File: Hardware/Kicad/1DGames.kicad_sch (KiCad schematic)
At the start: 0 parts

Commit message: Inline accessors, small cleanups, removed empty destructors
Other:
- sheet I2S Sound (page 4) renamed Audio (page 4) (pagina 4)
- sheet players renamed TM1637 & Joysticks
- note added: "AUDIO"
- note removed: "I2S SOUND"
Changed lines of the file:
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@@
 		)
 	)
-	(text "I2S SOUND"
+	(text "AUDIO"
 		(exclude_from_sim no)
 		(at 39.624 86.868 0)
@@
 			(color 0 0 0 0)
 		)
-		(property "Sheetname" "I2S Sound (page 4)"
+		(property "Sheetname" "Audio (page 4) (pagina 4)"
 			(at 24.13 90.7284 0)
 			(show_name no)
@@
 			(color 0 0 0 0)
 		)
-		(property "Sheetname" "players"
+		(property "Sheetname" "TM1637 & Joysticks"
 			(at 167.64 81.8384 0)
 			(show_name no)

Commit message: New architecture, L1 composition finished, probably, on ESP32
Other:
- sheet ESP32 & SPI ports: added MCP23017_INT_AB; removed none
- sheet I2C ports: added MCP23017_INT_AB; removed none
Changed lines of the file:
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@@
+	(wire
+		(pts
+			(xy 165.1 50.8) (xy 196.85 50.8)
+		)
+		(stroke
+			(width 0)
+			(type default)
+		)
+	)
 	(wire
 		(pts
@@
 	(wire
 		(pts
+			(xy 19.05 185.42) (xy 19.05 208.28)
+		)
+		(stroke
+			(width 0)
+			(type default)
+		)
+	)
+	(wire
+		(pts
 			(xy 143.51 107.95) (xy 152.4 107.95)
 		)
@@
 	(wire
 		(pts
+			(xy 24.13 185.42) (xy 19.05 185.42)
+		)
+		(stroke
+			(width 0)
+			(type default)
+		)
+	)
+	(wire
+		(pts
 			(xy 67.31 96.52) (xy 50.8 96.52)
 		)
@@
 	(wire
 		(pts
+			(xy 196.85 208.28) (xy 196.85 50.8)
+		)
+		(stroke
+			(width 0)
+			(type default)
+		)
+	)
+	(wire
+		(pts
 			(xy 67.31 184.15) (xy 161.29 184.15)
 		)
@@
 		(pts
 			(xy 90.17 110.49) (xy 97.79 110.49)
+		)
+		(stroke
+			(width 0)
+			(type default)
+		)
+	)
+	(wire
+		(pts
+			(xy 19.05 208.28) (xy 196.85 208.28)
 		)
 		(stroke
@@
 			)
 		)
+		(pin "MCP23017_INT_AB" input
+			(at 24.13 185.42 180)
+			(effects
+				(font
+					(size 1.27 1.27)
+				)
+				(justify left)
+			)
+		)
 		(instances
 			(project "1DGames"
@@
 	(sheet
 		(at 167.64 82.55)
-		(size 29.21 66.04)
+		(size 26.67 66.04)
 		(exclude_from_sim no)
 		(in_bom yes)
@@
 			(effects
 				(font
+					(size 1.27 1.27)
+				)
+				(justify right)
+			)
+		)
+		(pin "MCP23017_INT_AB" input
+			(at 165.1 50.8 0)
+			(effects
+				(font

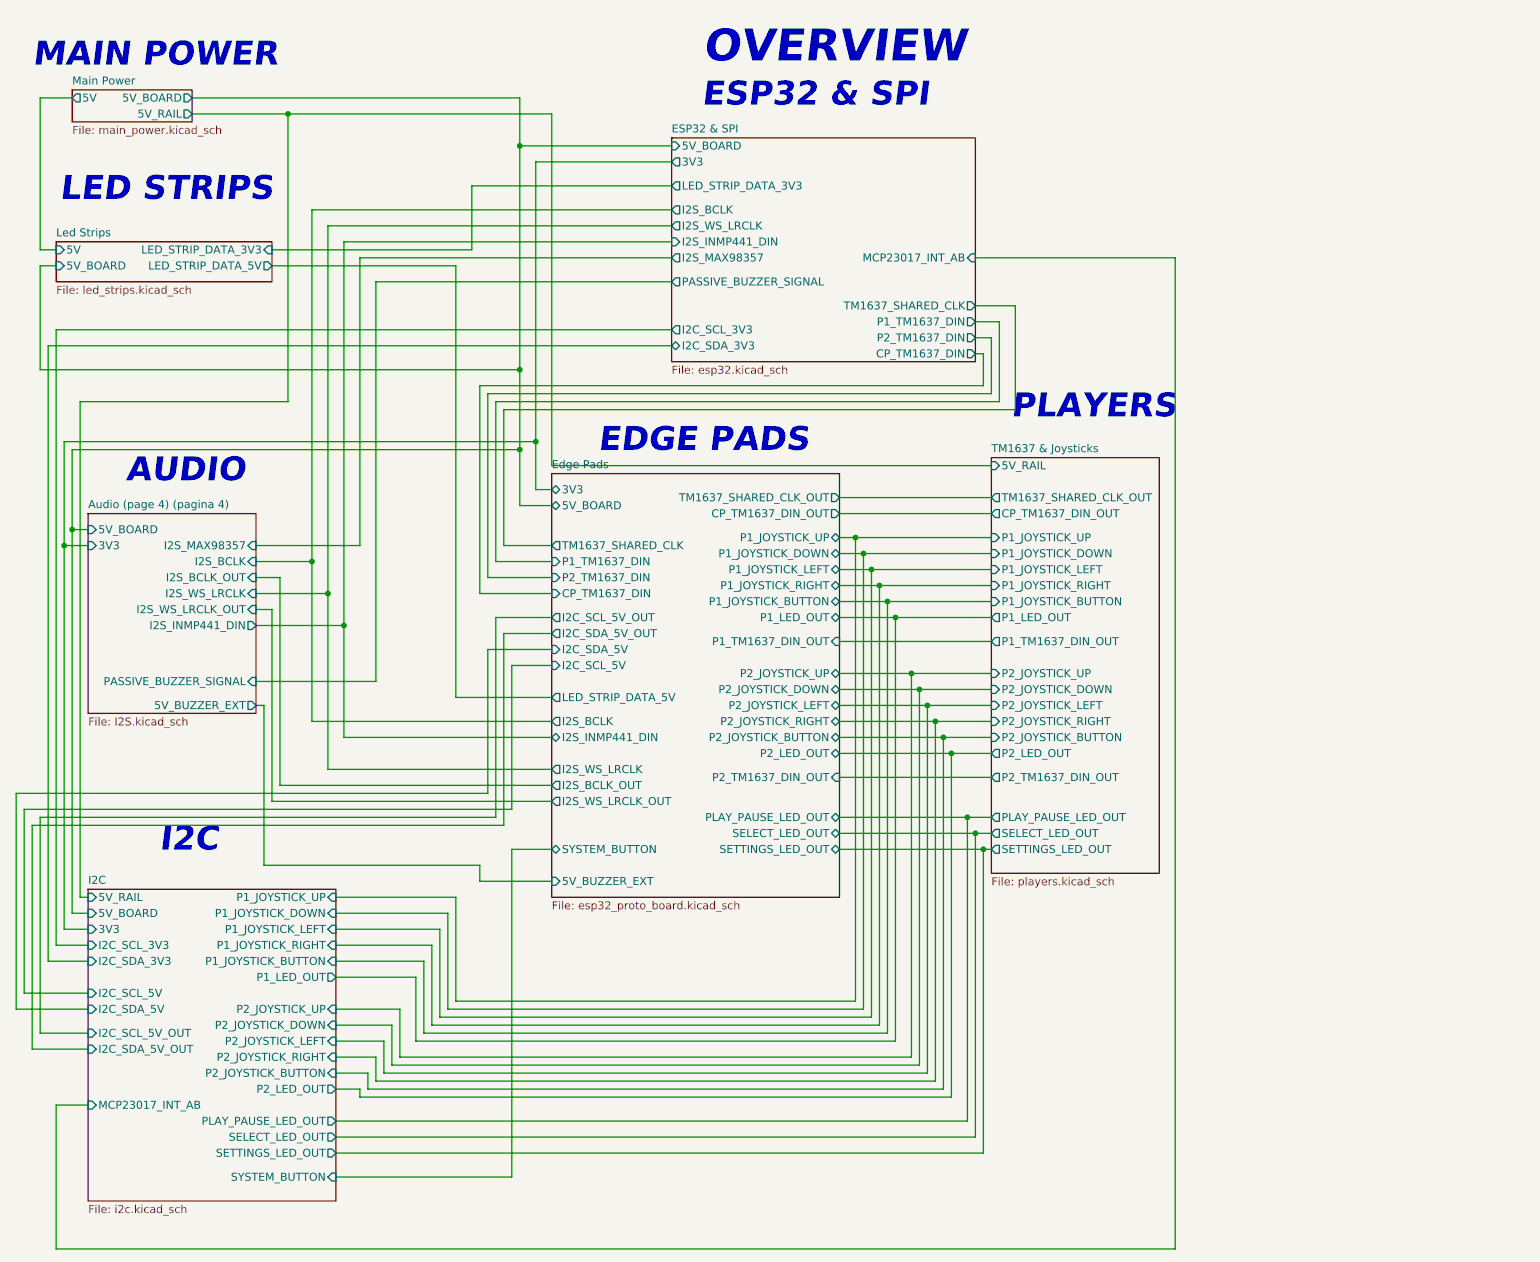
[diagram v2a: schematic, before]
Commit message: Broken code, halfway joystick gdi
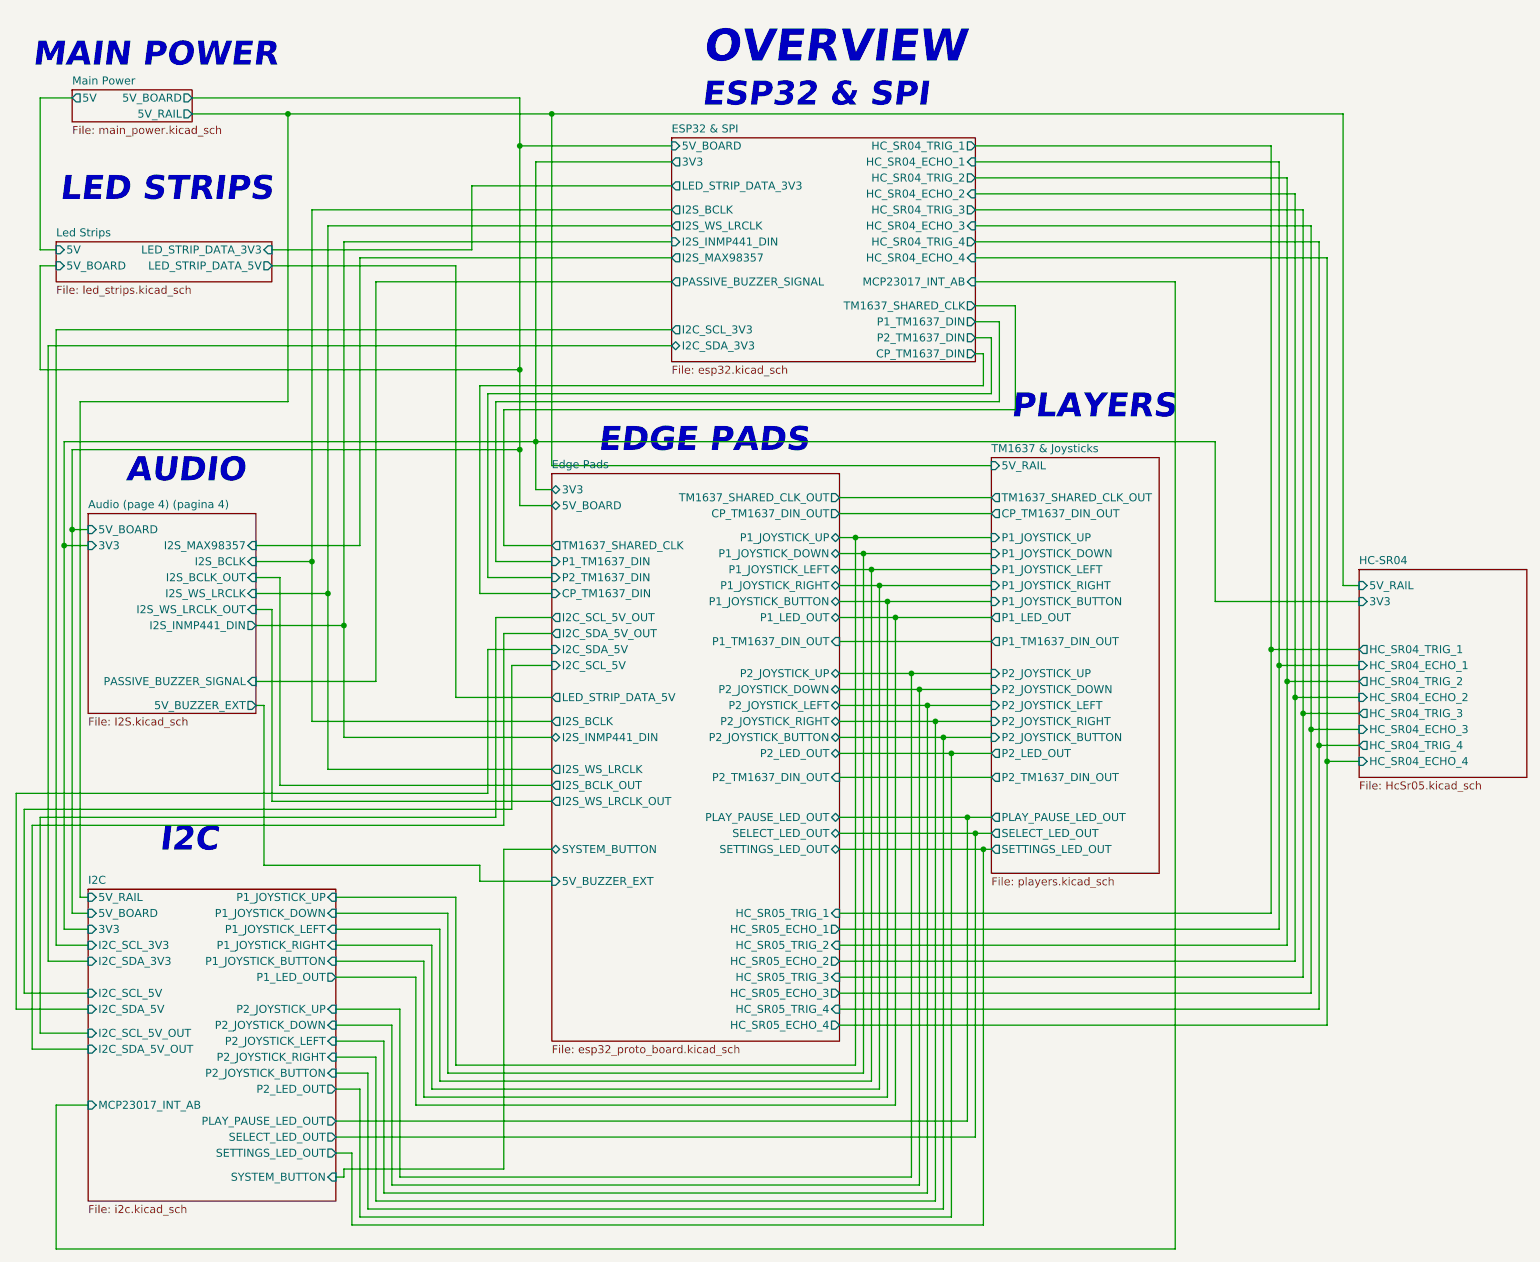
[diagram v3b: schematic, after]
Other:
- added sheet HC-SR04 (HcSr05.kicad_sch)
- sheet ESP32 & SPI ports: added HC_SR04_ECHO_1, HC_SR04_ECHO_2, HC_SR04_ECHO_3, HC_SR04_ECHO_4, HC_SR04_TRIG_1, HC_SR04_TRIG_2, HC_SR04_TRIG_3, HC_SR04_TRIG_4; removed none
- sheet Edge Pads ports: added HC_SR05_ECHO_1, HC_SR05_ECHO_2, HC_SR05_ECHO_3, HC_SR05_ECHO_4, HC_SR05_TRIG_1, HC_SR05_TRIG_2, HC_SR05_TRIG_3, HC_SR05_TRIG_4; removed none
